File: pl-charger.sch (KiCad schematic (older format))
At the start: 104 parts, among them J10 Charger, J11 Seven-segment, J12 LOAD, J8 Prog, J9 Button, Q13 MMBT2222A, Q14 MMBT2222A, Q15 MMBT2222A, Q16 MMBT2222A, Q17 MMBT2222A, Q18 PHD45N03LTA, Q19 PHD45N03LTA, Q20 MMBT2222A, U5 L78L05_SOT89, U6 ATmega88PA-AU, U7 LTC1733EMSEPBF, Y2 Crystal

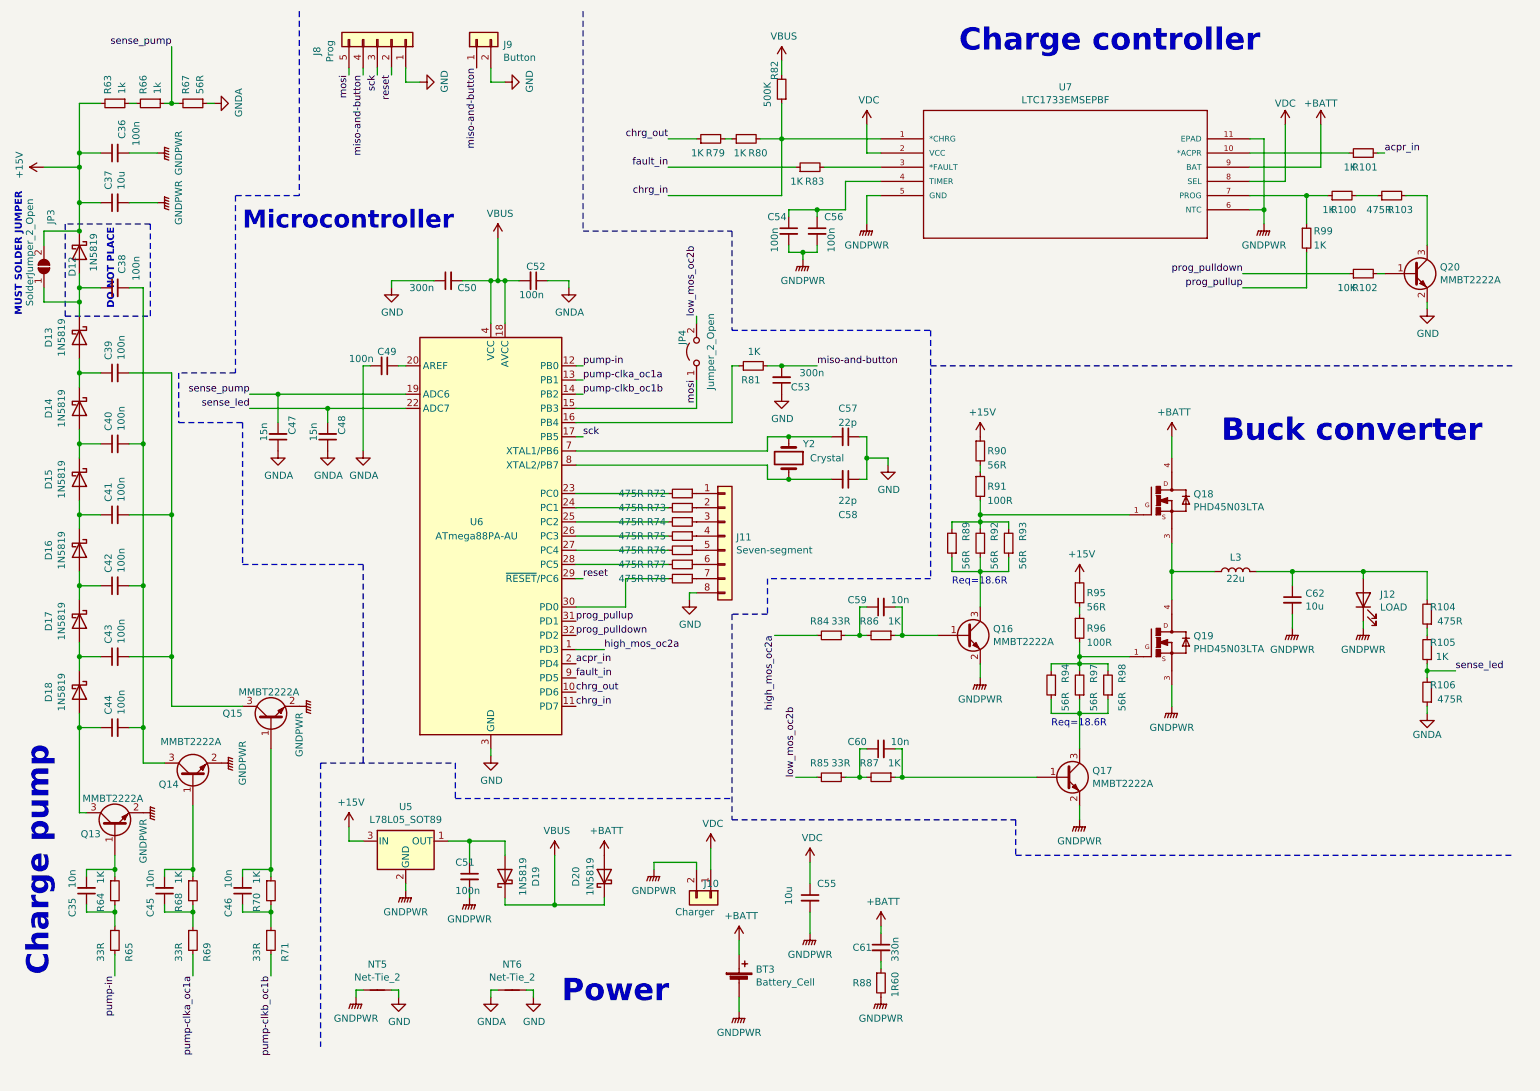
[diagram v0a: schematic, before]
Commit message: Fixed hierarchical sheet for microcontroller unit
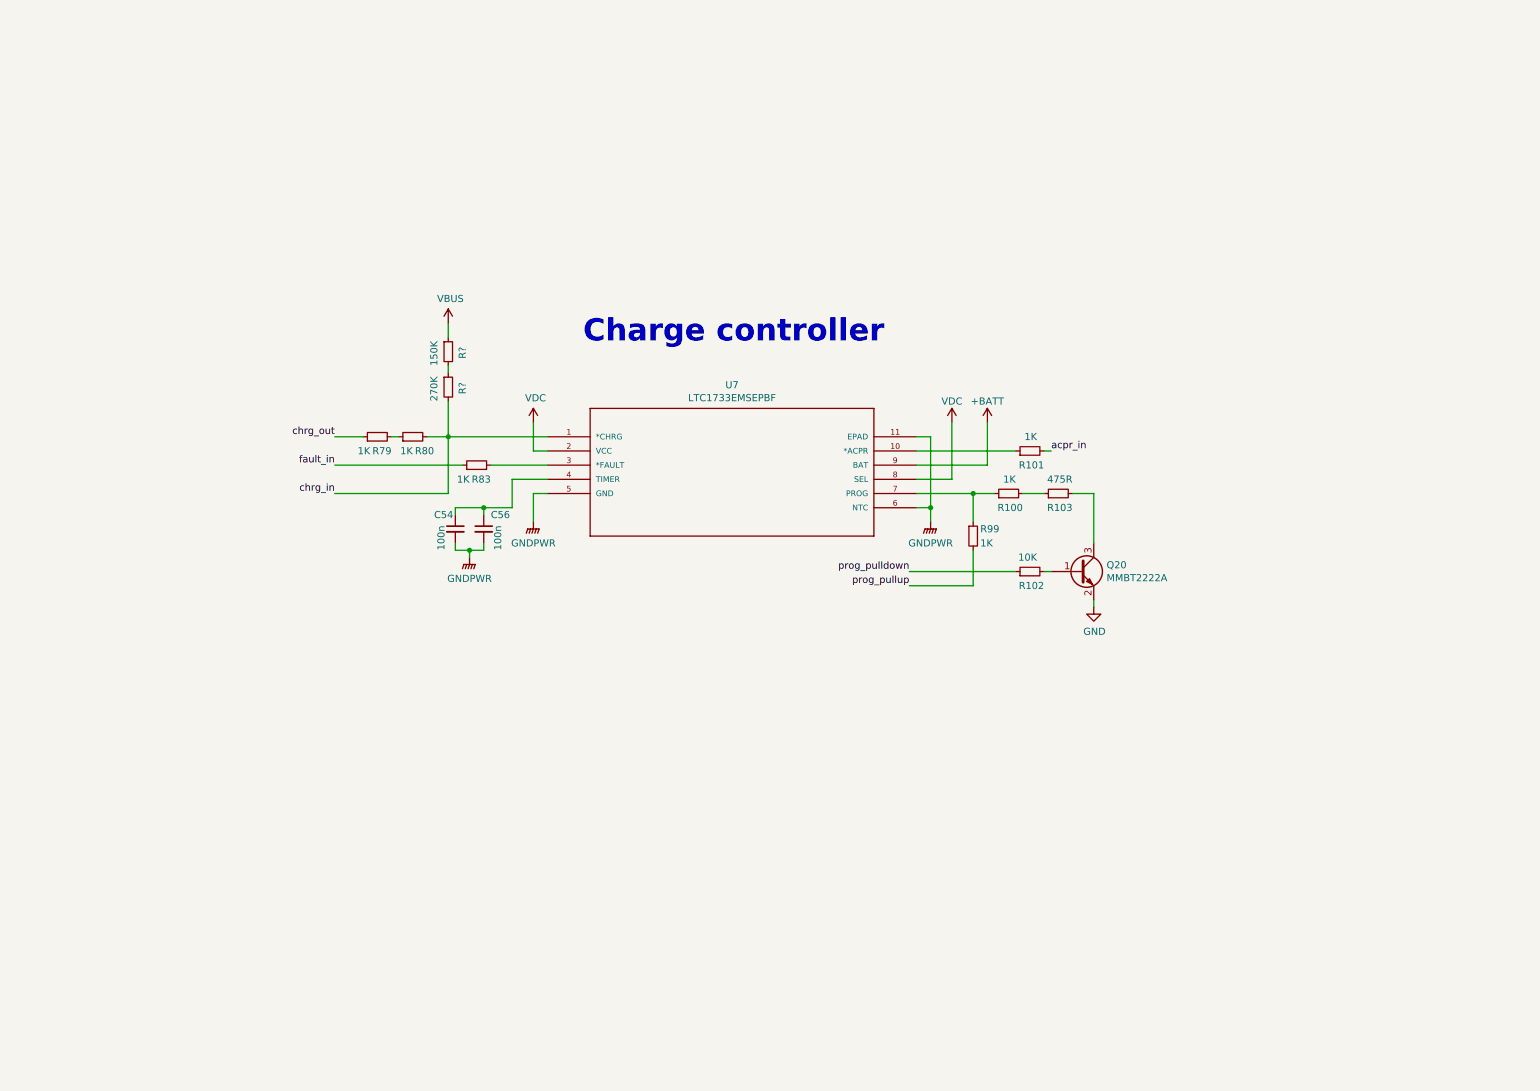
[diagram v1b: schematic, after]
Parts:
- removed BT3: Battery_Cell, Connector_PinHeader_2.54mm:PinHeader_1x02_P2.54mm_Vertical, symbol portable-light-rescue:Battery_Cell-Device
- removed C35, C45, C46, C59, C60: 10n, Capacitor_SMD:C_1206_3216Metric_Pad1.42x1.75mm_HandSolder, symbol portable-light-rescue:C_Small-Device
- removed C36, C38, C39, C40, C41, C42, C43, C44, C49, C51, C52: 100n, Capacitor_SMD:C_1206_3216Metric_Pad1.42x1.75mm_HandSolder, symbol portable-light-rescue:C_Small-Device
- removed C37, C55, C62: 10u, Capacitor_THT:C_Radial_D5.0mm_H7.0mm_P2.00mm, symbol portable-light-rescue:C_Small-Device
- removed C47, C48: 15n, Capacitor_SMD:C_1206_3216Metric_Pad1.42x1.75mm_HandSolder, symbol portable-light-rescue:C_Small-Device
- removed C50, C53: 300n, Capacitor_SMD:C_0805_2012Metric_Pad1.15x1.40mm_HandSolder, symbol portable-light-rescue:C_Small-Device
- removed C57, C58: 22p, Capacitor_SMD:C_1206_3216Metric_Pad1.42x1.75mm_HandSolder, symbol portable-light-rescue:C_Small-Device
- removed C61: 330n, Capacitor_SMD:C_1206_3216Metric_Pad1.42x1.75mm_HandSolder, symbol portable-light-rescue:C_Small-Device
- removed D12, D13, D14, D15, D16, D17, D18: 1N5819, Diode_SMD:D_SMA_Handsoldering, symbol portable-light-rescue:1N5819-Diode
- removed D19, D20: 1N5819, Diode_THT:D_DO-41_SOD81_P12.70mm_Horizontal, symbol portable-light-rescue:1N5819-Diode
- removed J10: Charger, Connector_PinHeader_2.54mm:PinHeader_1x02_P2.54mm_Vertical, symbol portable-light-rescue:Conn_01x02-Connector_Generic
- removed J11: Seven-segment, Ribbon_Cable:Ribbon_8, symbol portable-light-rescue:Conn_01x08-Connector_Generic
- removed J12: LOAD, Connector_PinHeader_2.54mm:PinHeader_1x02_P2.54mm_Vertical, symbol portable-light-rescue:LED-Device
- removed J8: Prog, Connector_PinHeader_2.54mm:PinHeader_1x05_P2.54mm_Vertical, symbol portable-light-rescue:Conn_01x05-Connector_Generic
- removed J9: Button, Ribbon_Cable:Ribbon_2, symbol portable-light-rescue:Conn_01x02-Connector_Generic
- removed JP3: SolderJumper_2_Open, Jumper:SolderJumper-2_P1.3mm_Open_TrianglePad1.0x1.5mm, symbol portable-light-rescue:SolderJumper_2_Open-Jumper
- removed JP4: Jumper_2_Open, Jumper:SolderJumper-2_P1.3mm_Open_RoundedPad1.0x1.5mm, symbol portable-light-rescue:Jumper_2_Open-Jumper
- removed L3: 22u, Capacitor_THT:CP_Radial_D8.0mm_P5.00mm, symbol portable-light-rescue:L-Device
- removed NT5, NT6: Net-Tie_2, NetTie:NetTie-2_SMD_Pad0.5mm, symbol portable-light-rescue:Net-Tie_2-Device
- removed Q13, Q14, Q15, Q16, Q17: MMBT2222A, Package_TO_SOT_SMD:SOT-23, symbol portable-light-rescue:MMBT3904-Transistor_BJT
- removed Q18, Q19: PHD45N03LTA, UniX_Generic:DPAK, symbol portable-light-rescue:PHD45N03LTA-PHD45N03LTA
- removed R104, R72, R73, R74, R75, R76, R77, R78: 475R, Resistor_SMD:R_1206_3216Metric_Pad1.42x1.75mm_HandSolder, symbol portable-light-rescue:R_Small-Device
- removed R105, R64, R68, R70, R81, R86, R87: 1K, Resistor_SMD:R_0603_1608Metric_Pad1.05x0.95mm_HandSolder, symbol portable-light-rescue:R_Small-Device
- removed R106: 475R, Resistor_SMD:R_0805_2012Metric_Pad1.15x1.40mm_HandSolder, symbol portable-light-rescue:R_Small-Device
- removed R63, R66: 1k, Resistor_SMD:R_0603_1608Metric_Pad1.05x0.95mm_HandSolder, symbol portable-light-rescue:R_Small-Device
- removed R65, R69, R71, R84, R85: 33R, Resistor_SMD:R_0805_2012Metric_Pad1.15x1.40mm_HandSolder, symbol portable-light-rescue:R_Small-Device
- removed R67, R89, R90, R92, R93, R94, R95, R97, R98: 56R, Resistor_SMD:R_0805_2012Metric_Pad1.15x1.40mm_HandSolder, symbol portable-light-rescue:R_Small-Device
- removed R82: 500K, Resistor_THT:R_Axial_DIN0309_L9.0mm_D3.2mm_P12.70mm_Horizontal, symbol portable-light-rescue:R_Small-Device
- removed R88: 1R60, Resistor_SMD:R_0805_2012Metric_Pad1.15x1.40mm_HandSolder, symbol portable-light-rescue:R_Small-Device
- removed R91, R96: 100R, Resistor_SMD:R_1206_3216Metric_Pad1.42x1.75mm_HandSolder, symbol portable-light-rescue:R_Small-Device
- removed U5: L78L05_SOT89, Package_TO_SOT_SMD:SOT-89-3, symbol portable-light-rescue:L78L05_SOT89-Regulator_Linear
- removed U6: ATmega88PA-AU, Package_QFP:TQFP-32_7x7mm_P0.8mm, symbol portable-light-rescue:ATmega88PA-AU-MCU_Microchip_ATmega
- removed Y2: Crystal, Crystal:Crystal_SMD_HC49-SD, symbol portable-light-rescue:Crystal-Device
- added R?: 150K, Resistor_SMD:R_0603_1608Metric_Pad1.05x0.95mm_HandSolder, symbol portable-light-rescue:R_Small-Device
- added R?: 270K, Resistor_SMD:R_0603_1608Metric_Pad1.05x0.95mm_HandSolder, symbol portable-light-rescue:R_Small-Device
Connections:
- net VBUS: now also R?.1
- net chrg_in: now also R?.2
- new net: R?.1, R?.2
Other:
- note removed: "Buck converter"
- note removed: "Charge pump"
- note removed: "DO NOT PLACE"
- note removed: "MUST SOLDER JUMPER"
- note removed: "Microcontroller"
- note removed: "Power"
- note removed: "Req=18.6R"
- moved on the sheet: C54, C56, Q20, R100, R101, R102, R103, R79, R80, R83, R99, U7

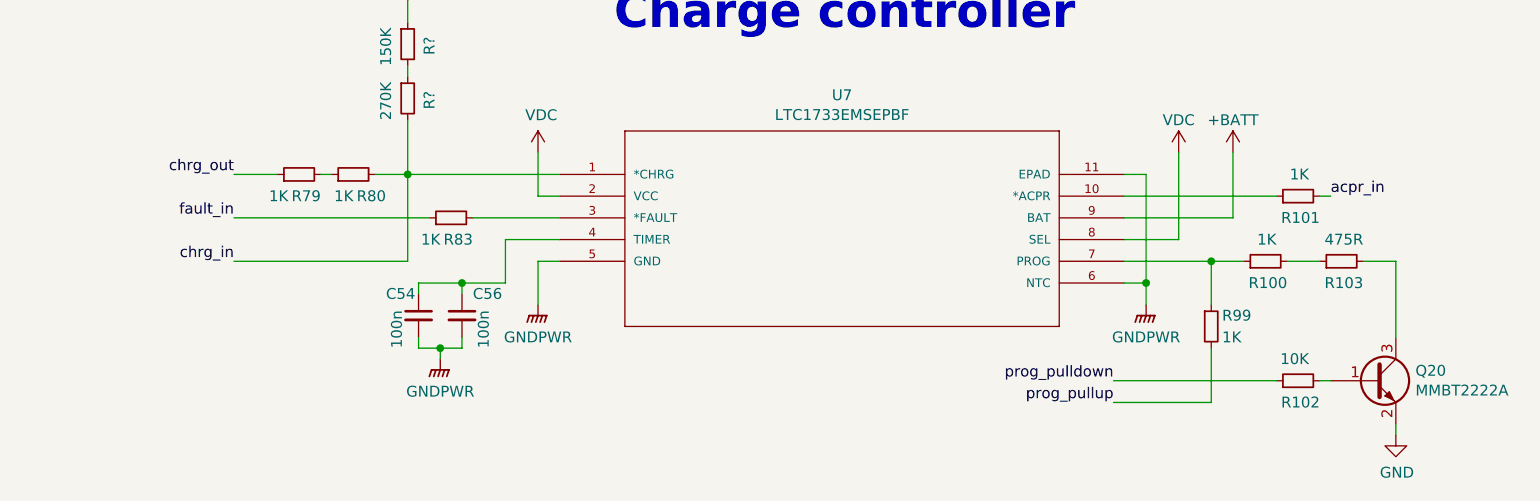
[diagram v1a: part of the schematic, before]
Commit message: Charger hierarchical sheet fixed
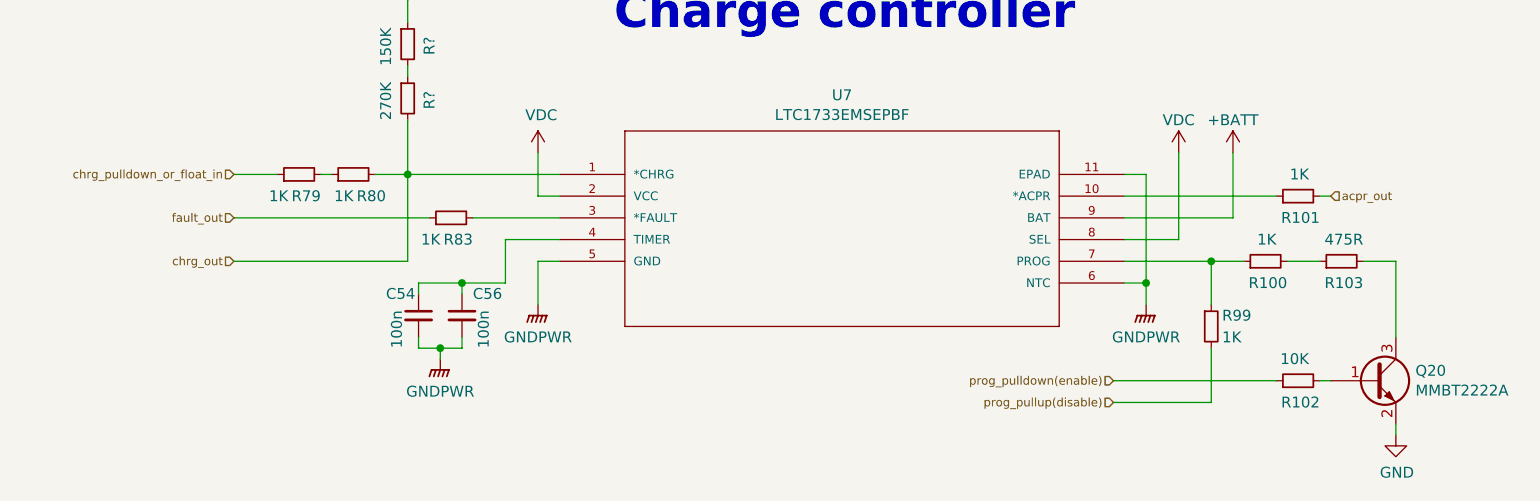
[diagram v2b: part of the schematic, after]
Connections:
- net chrg_in is gone; now on net chrg_out: R80.2, R?.2, U7.1 (*CHRG)
- net chrg_out: no longer R79.1
- net acpr_in renamed acpr_out
- net fault_in renamed fault_out
- net prog_pulldown renamed prog_pulldown(enable)
- net prog_pullup renamed prog_pullup(disable)
- new net chrg_pulldown_or_float_in: R79.1
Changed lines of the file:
@@
 Wire Wire Line
 	2850 3500 3050 3500
-Text Label 2850 3500 2    50   ~ 0
-chrg_out
-Text Label 2850 3900 2    50   ~ 0
-chrg_in
 $Comp
 L portable-light-rescue:VDC-power #PWR0177
@@
 	0    -1   -1   0
 $EndComp
-Text Label 7900 3600 0    50   ~ 0
-acpr_in
 Wire Wire Line
 	7850 3600 7900 3600
@@
 	0    -1   -1   0
 $EndComp
-Text Label 2850 3700 2    50   ~ 0
-fault_in
 Wire Wire Line
 	3500 3500 3650 3500
@@
 Wire Wire Line
 	7350 4550 6900 4550
-Text Label 6900 4450 2    50   ~ 0
-prog_pulldown
-Text Label 6900 4550 2    50   ~ 0
-prog_pullup
 Wire Wire Line
 	8200 4700 8200 4650
@@
 Wire Wire Line
 	3650 3050 3650 3000
+Text HLabel 6900 4450 0    39   Input ~ 0
+prog_pulldown(enable)
+Text HLabel 6900 4550 0    39   Input ~ 0
+prog_pullup(disable)
+Text HLabel 2850 3900 0    39   Input ~ 0
+chrg_out
+Text HLabel 2850 3500 0    39   Input ~ 0
+chrg_pulldown_or_float_in
+Text HLabel 7900 3600 2    39   Input ~ 0
+acpr_out
+Text HLabel 2850 3700 0    39   Input ~ 0
+fault_out
 $EndSCHEMATC

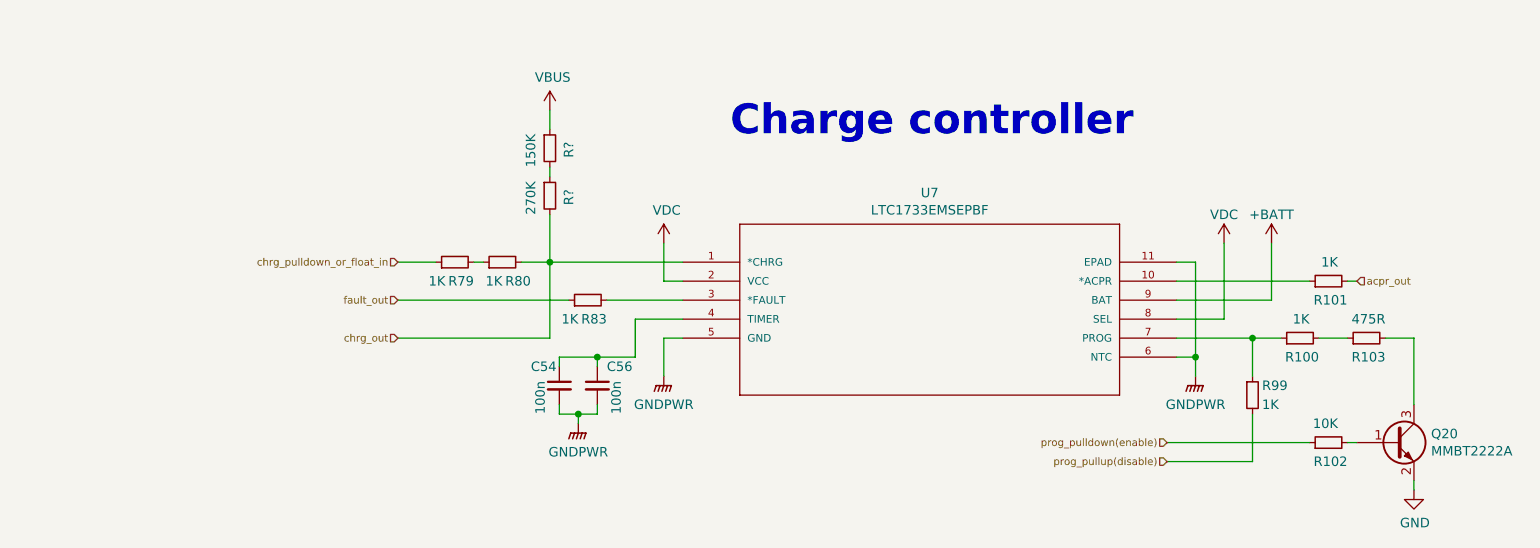
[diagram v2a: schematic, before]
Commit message: Schematic's overall structure is finished
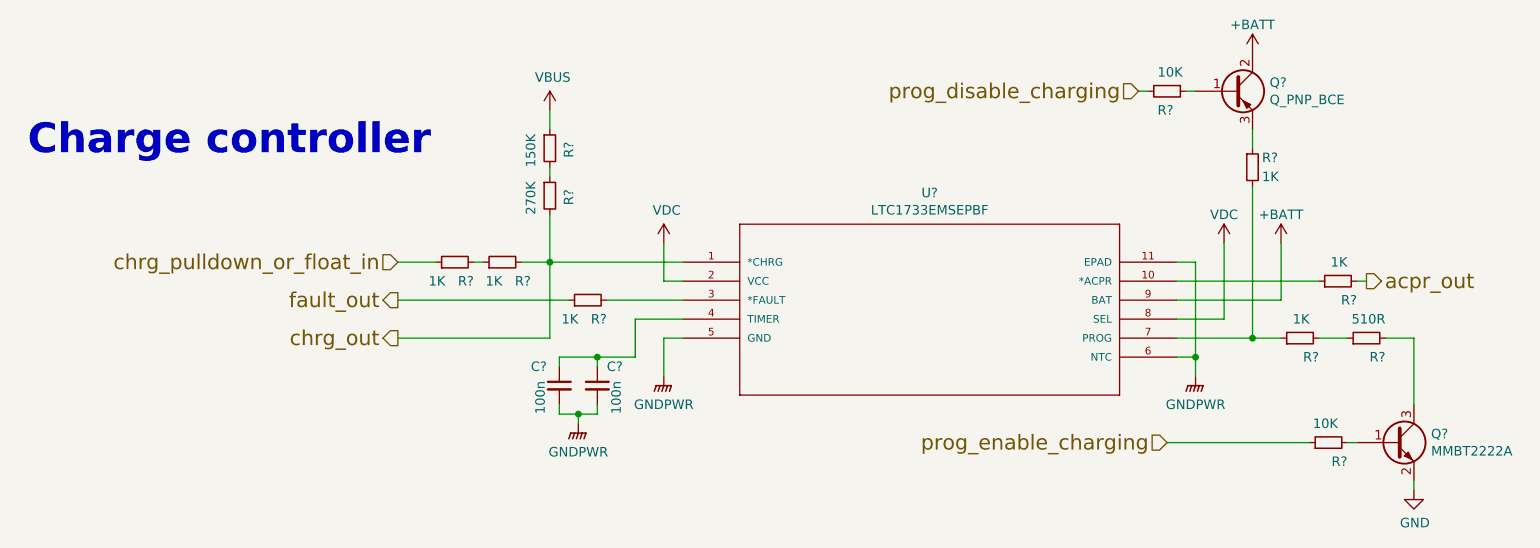
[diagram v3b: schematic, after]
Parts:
- added Q?: Q_PNP_BCE, symbol Device:Q_PNP_BCE
- added R?: 10K, Resistor_SMD:R_0603_1608Metric_Pad1.05x0.95mm_HandSolder, symbol portable-light-rescue:R_Small-Device
- R?: renamed from R103; value 475R -> 510R; footprint Resistor_SMD:R_1206_3216Metric_Pad1.42x1.75mm_HandSolder -> Resistor_SMD:R_0805_2012Metric_Pad1.15x1.40mm_HandSolder
- renumbered C54 to C?, C56 to C?, Q20 to Q?, R83 to R?, R100 to R?, R102 to R?, R79 to R?, R101 to R?, R99 to R?, R80 to R?, U7 to U?
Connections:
- net prog_pullup(disable) is gone; now on an unnamed net: R?.2
- net +BATT: now also Q?.2 (C)
- net at R?.1, U?.7 (PROG): no longer R?.1
- net prog_pulldown(enable) renamed prog_enable_charging
- new net: Q?.3 (E), R?.1
- new net: Q?.1 (B), R?.1
- new net prog_disable_charging: R?.2
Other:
- moved on the sheet: R?
